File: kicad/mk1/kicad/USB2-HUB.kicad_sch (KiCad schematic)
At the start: 30 parts, among them J5 690-008-221-904, J6 Conn_02x05_Odd_Even, U11 FSUSB42MUX, U12 USB2514B-I/M2, U14 AP22653W6, Y3 24MHz

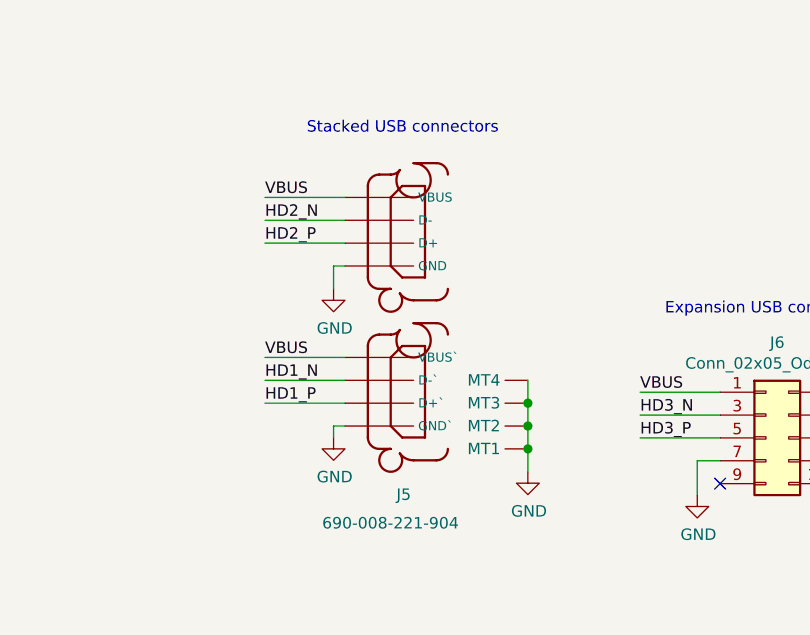
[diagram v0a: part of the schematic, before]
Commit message: work on schematics
* add power rail
* import CM4 related part
* design most of the BMC-PHY part
* create new library/footprint for rp t113-s3 SOM
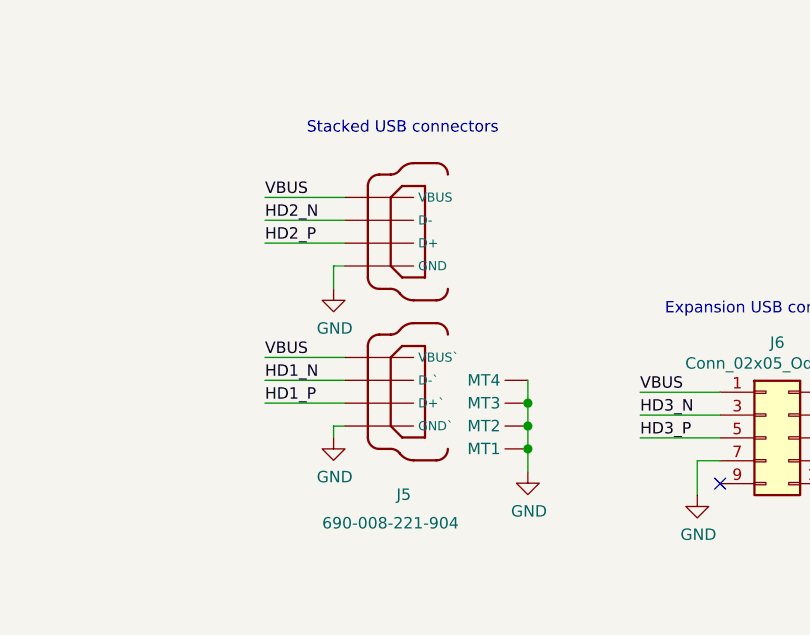
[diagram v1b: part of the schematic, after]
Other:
- moved on the sheet: J5
